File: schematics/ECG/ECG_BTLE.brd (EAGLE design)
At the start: 30 x 30 mm, 29 parts, among them IC1 ADS1293, IC3 MCP1703, IC4 CC2541

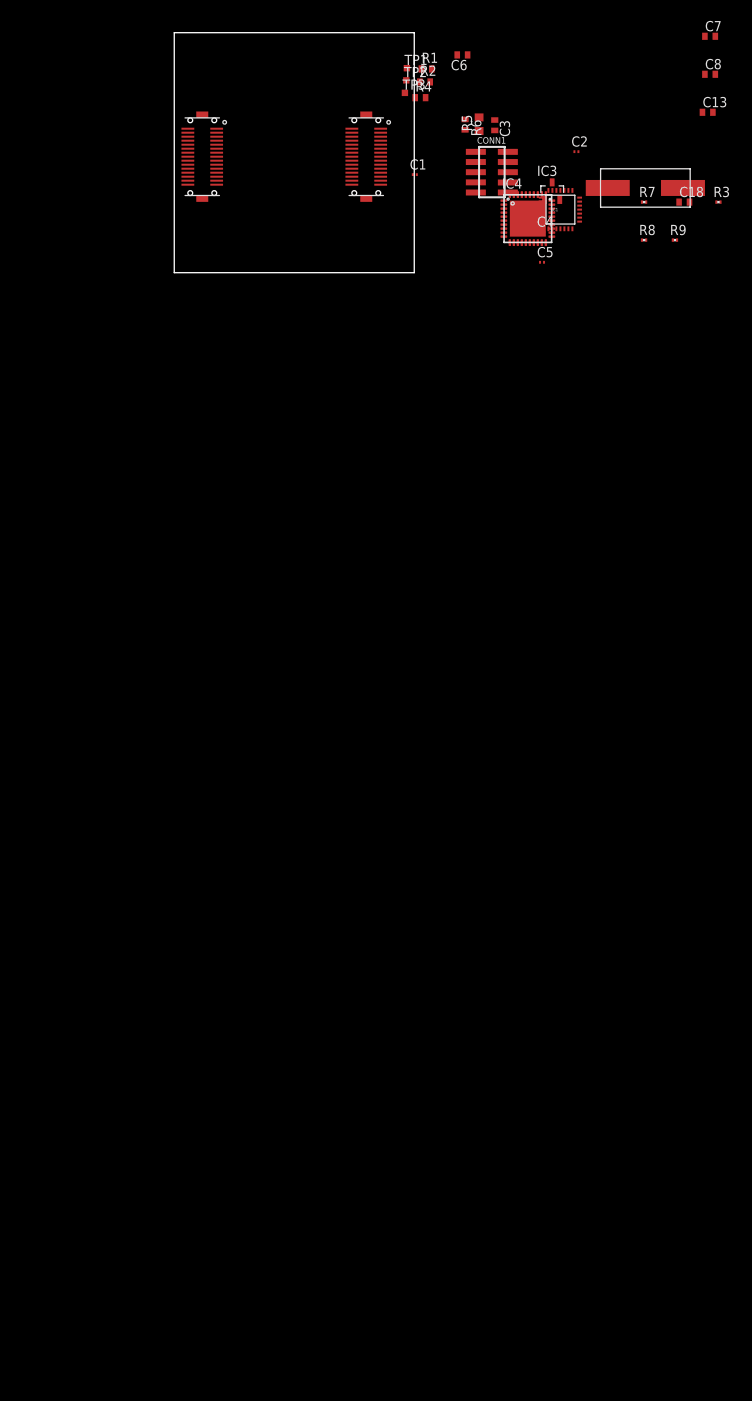
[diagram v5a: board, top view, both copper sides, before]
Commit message: updated board, added BOM template
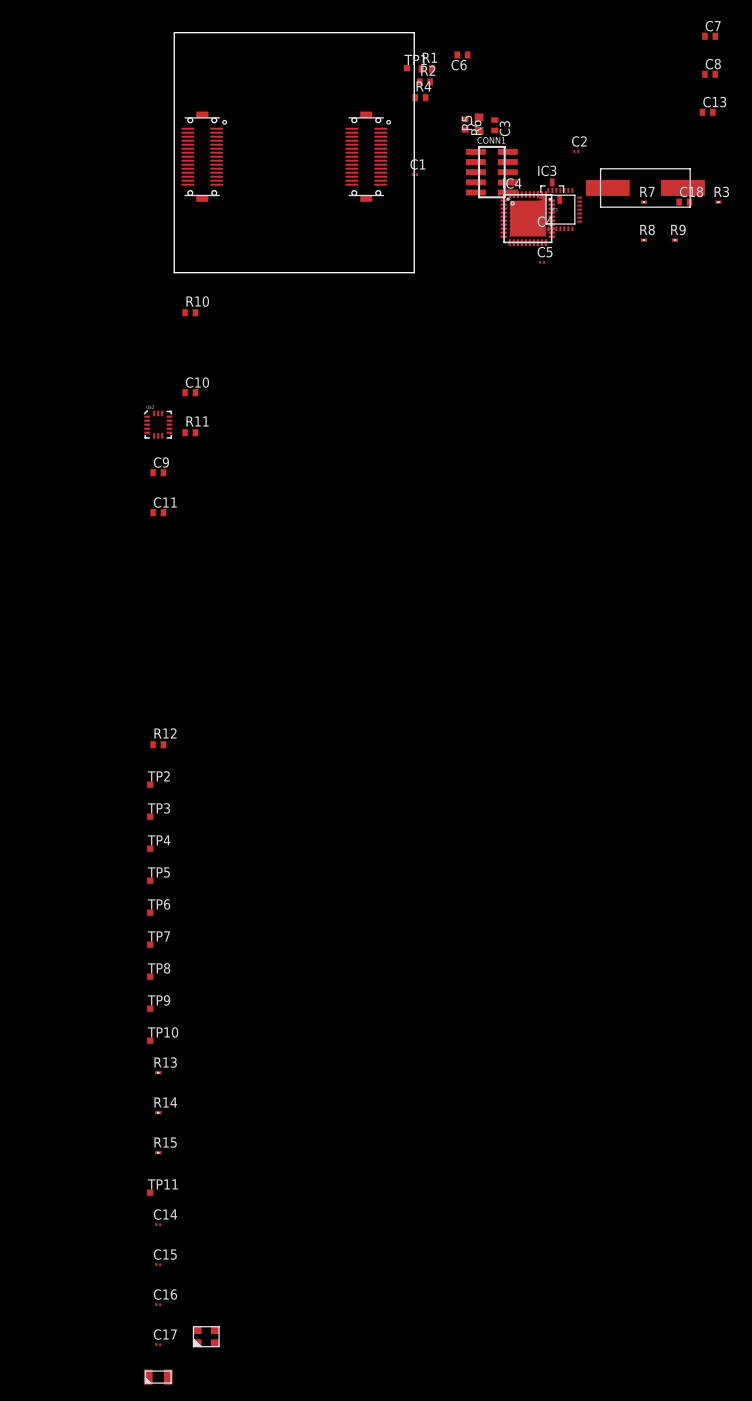
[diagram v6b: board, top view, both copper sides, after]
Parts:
- added C10: 1uF, rcl:C0402
- added C11: 10uF, rcl:C0402
- added C14, C15: 12pF, rcl:C0201
- added C16, C17: 10pF, rcl:C0201
- added C9: 0.1uF, rcl:C0402
- added R10, R11: 1M, resistor:R0402
- added R12: 0, resistor:R0402
- added R13, R14: 100K, rcl:R0201
- added R15: 0, rcl:R0201
- added TP10, TP11, TP4, TP5, TP6, TP7, TP8, TP9: TPSTP08SQ, testpad:TP08SQ
- added U$2: LIS3DH, st:LGA16-3MM
- added X1-X: XTAL-2SMD, ecs:2-SMD
- added X2: XTAL_403, cts:4-SMD
- C1, C2: value (none) -> 22pF
- C3: value 1nF (01016D102KAT2A) -> 1.5nF
- R5: value 10M (RK73H1HTTC1005F) -> 1M
- R6: value 10K (RK73B1FTTBL103J) -> 100K
- moved TP3 95.9 mm to (-3.00, -68.0)
- moved TP2 93.7 mm to (-3.00, -64.0)
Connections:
- removed net 16XCLK: IC4.7
- removed net GATE_R: IC4.14
- removed net GATE_T: IC4.15
- removed net IR_SD: IC4.19
- removed net MCP_RST: IC4.18
- removed net MCU_UART_RX: IC4.17
- removed net MCU_UART_TX: IC4.16
- removed net N$3: CONN1.7
- removed net N$4: CONN1.1
- removed net N$7: C5.1, IC3.2
- removed net P0_6: IC4.13
- removed net P0_7: IC4.12
- removed net VCC_CONTROL: IC4.11
- removed net VDD: C7.1, C8.1, IC1.22, IC1.28
- new net ACCEL_INT1: IC4.12, U$2.11
- new net ALARMB: IC1.15, IC4.18, TP10.TP
- new net BATT_SCALED: IC4.13, R13.1, R14.2
- new net DRDYB: IC1.20, IC4.19, TP5.TP
- new net IN3: IC1.3, R2.2
- new net LL: R2.1, TP3.TP
- new net N$11: C10.1, IC1.11, IC1.12
- new net N$12: IC1.13, R11.2
- new net N$13: U$2.1
- new net N$5: IC1.25, R10.1
- new net SPI_CSB: IC1.16, IC4.15, TP9.TP, U$2.8
- new net SPI_SCLK: IC1.17, IC4.14, TP8.TP, U$2.4
- new net SPI_SDI: IC1.18, IC4.17, TP7.TP, U$2.6
- new net SPI_SDO: IC1.19, IC4.16, TP6.TP, U$2.7
- new net XTAL1: C2.2, IC1.23, U$1.2
- new net XTAL2: C1.2, IC1.24, U$1.1
- net BATT+: now also R13.2
- net GND: now also C10.2, C11.2, C14.2, C15.2, C16.2, C17.2, C9.2, CONN1.1, R14.1, U$2.10, U$2.12, U$2.5
- net IN2: now also R12.2; no longer R2.2
- net LA: now also R12.1; no longer R2.1
- net N$1: now also CONN1.9, R15.1; no longer CONN1.4
- net N$2: now also R15.2, TP11.TP; no longer CONN1.3
- net P2_1/DD: now also CONN1.4
- net P2_2/DC: now also CONN1.3
- net P2_3/32K_Q2: now also C14.1, X1-X.1
- net P2_4/32K_Q1: now also C15.1, X1-X.2
- net RESET_N: now also CONN1.7
- net RL: now also TP4.TP; no longer TP3.TP
- net VCC: now also C1.1, C11.1, C2.1, C5.1, C7.1, C8.1, C9.1, CONN1.2, IC1.22, IC1.28, IC3.2, R10.2, R11.1, U$2.14
- net XOSC_Q1: now also C16.1, X2.P1
- net XOSC_Q2: now also C17.1, X2.P3
